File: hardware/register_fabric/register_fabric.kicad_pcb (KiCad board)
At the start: 4 copper layers, 356 x 62.3 mm, 431 parts, among them J2 Conn_02x40_Odd_Even, J3 Conn_02x16_Odd_Even, J4 Conn_02x16_Odd_Even, J5 Conn_02x16_Odd_Even, J6 Conn_02x16_Odd_Even, J7 Conn_02x16_Odd_Even, J8 Conn_02x16_Odd_Even, J9 Conn_02x16_Odd_Even, Q109 IRLML6244, Q110 IRLML6402, Q111 IRLML6244, Q112 IRLML6402, Q113 IRLML6244, Q114 IRLML6402, Q115 IRLML6244, Q116 IRLML6402, Q117 IRLML6244, Q118 IRLML6402, Q119 IRLML6244, Q120 IRLML6402, Q121 IRLML6244, Q122 IRLML6402, Q123 IRLML6244, Q124 IRLML6402, Q125 IRLML6244, Q126 IRLML6402, Q127 IRLML6244, Q128 IRLML6402, Q129 IRLML6244, Q130 IRLML6402, Q131 IRLML6244, Q132 IRLML6402, Q133 IRLML6244, Q134 IRLML6402, Q135 IRLML6244, Q136 IRLML6402, Q137 IRLML6244, Q138 IRLML6402, Q139 IRLML6244, Q140 IRLML6402, Q141 IRLML6244, Q142 IRLML6402, Q143 IRLML6244, Q144 IRLML6402, Q145 IRLML6244, Q146 IRLML6402, Q147 IRLML6244, Q148 IRLML6402, Q149 IRLML6244, Q150 IRLML6402, Q151 IRLML6244, Q152 IRLML6402, Q153 IRLML6244, Q154 IRLML6402, Q155 IRLML6244, Q156 IRLML6402, Q157 IRLML6244, Q158 IRLML6402, Q159 IRLML6244, Q160 IRLML6402, Q161 IRLML6244, Q162 IRLML6402, Q163 IRLML6244, Q164 IRLML6402, Q165 IRLML6244, Q166 IRLML6402, Q167 IRLML6244, Q168 IRLML6402, Q169 IRLML6244, Q170 IRLML6402, Q171 IRLML6244, Q172 IRLML6402, Q173 IRLML6244, Q174 IRLML6402, Q175 IRLML6244, Q176 IRLML6402, Q177 IRLML6244, Q178 IRLML6402, Q179 IRLML6244, Q180 IRLML6402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

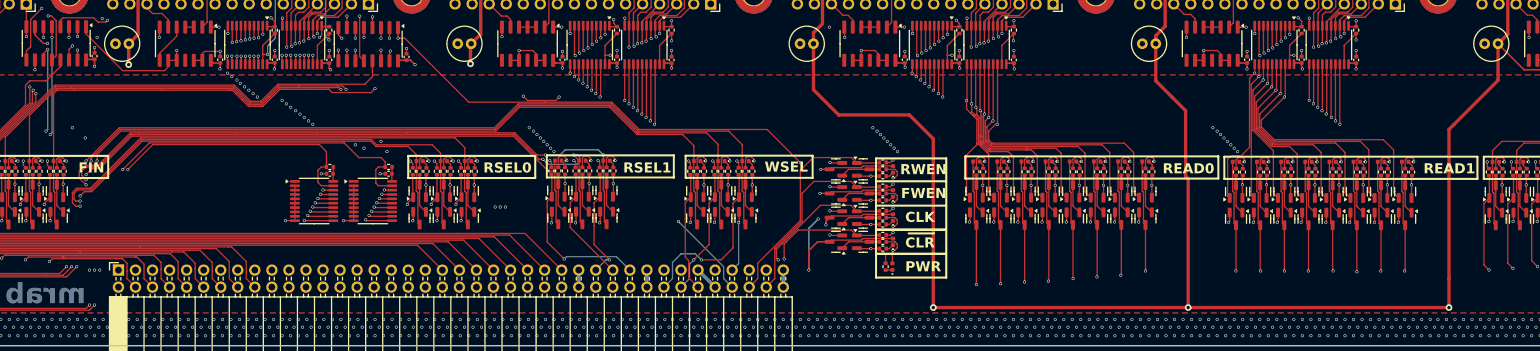
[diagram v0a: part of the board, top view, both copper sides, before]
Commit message: all PCBs passing all CRC & vibe checks
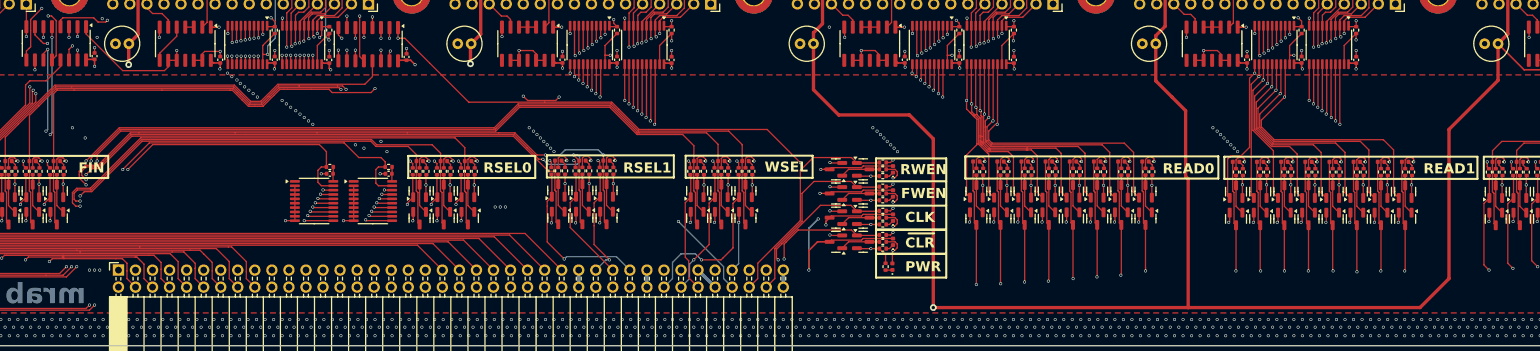
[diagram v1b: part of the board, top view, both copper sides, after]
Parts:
- R1, R10, R11, R12, R13, R14, R15, R16, R2, R21, R22, R23, R24, R25, R26, R27, R28, R29, R3, R30, R31, R32, R33, R34, R35, R36, R37, R38, R39, R4, R40, R41, R45, R46, R47, R48, R49, R5, R50, R51, R52, R6, R7, R8, R9: value 10K -> 100K
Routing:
- net +5V: track 1822.9 -> 1820.4 mm, vias 171 -> 169
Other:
- board text added: "Matzispatzi <3"
- board text added: "Wer das liest, ist doof."
- board text removed: "Wer das liest, ist doof"
